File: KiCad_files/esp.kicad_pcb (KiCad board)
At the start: 2 copper layers, 86 x 75 mm, 69 parts, among them J1 Conn_01x02_Pin, J2 USB4105-GF-A, J3 Conn_01x16_Pin, Q2 DMP3099L, SW1 SLW-171175-7A-N-D, U1 B3U-1000P, U12 ESP32-S3-MINI-1U, U13 BNO085, U2 1060, U7 LTC4412xS6

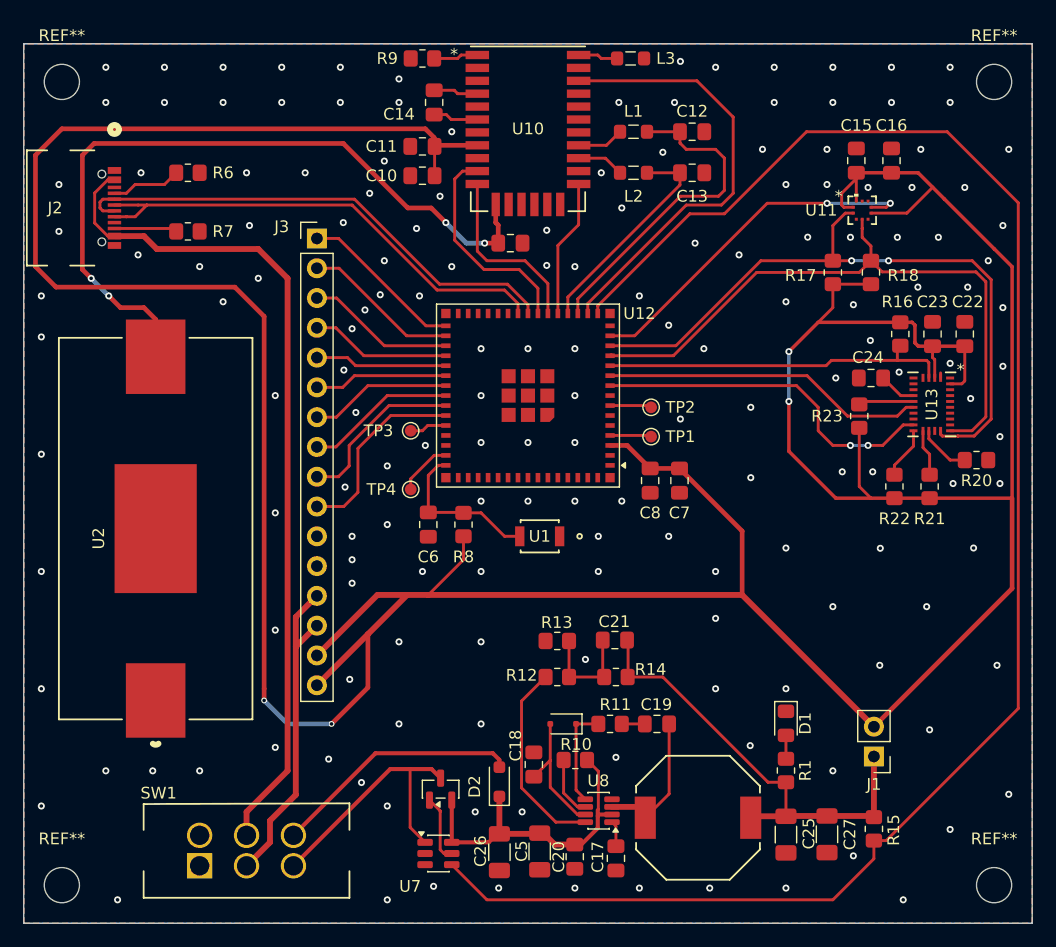
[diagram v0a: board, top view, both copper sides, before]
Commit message: power supply FB circuitry to better place
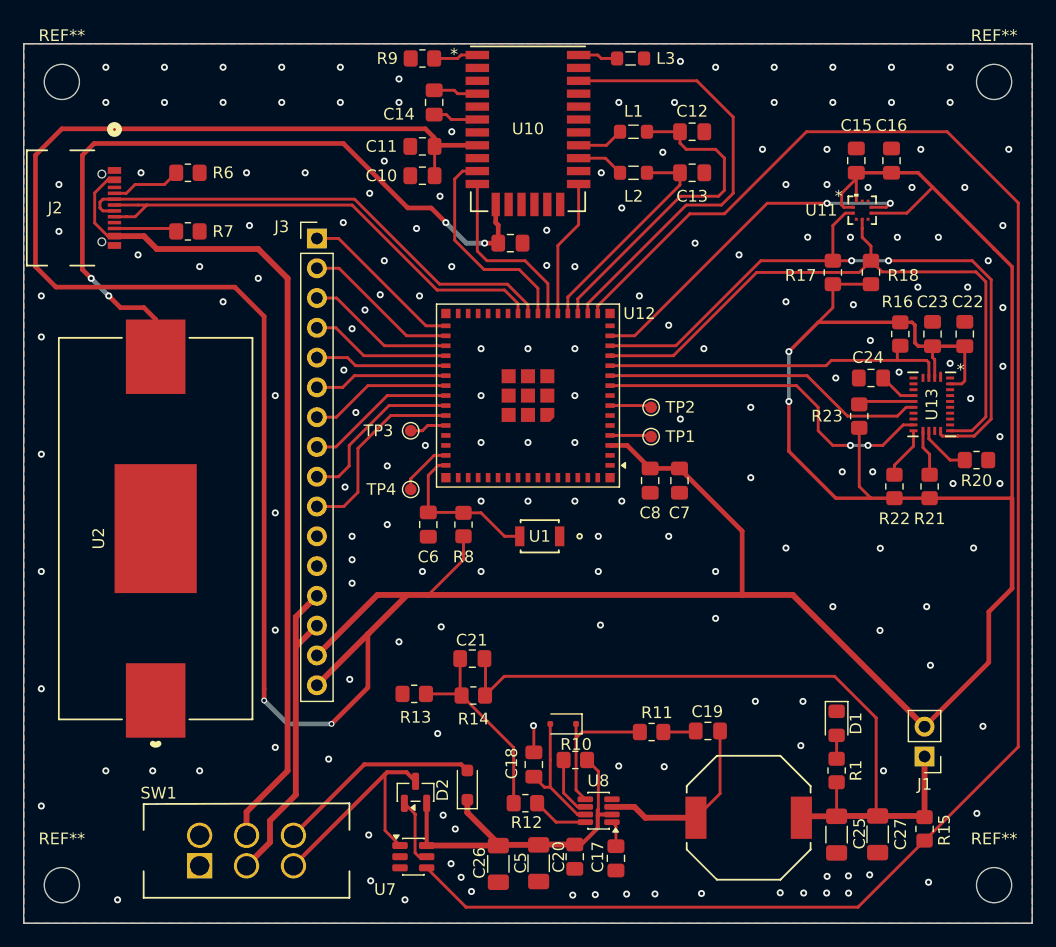
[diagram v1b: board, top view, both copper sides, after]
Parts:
- moved R13 13.0 mm to (115.3, 80.4)
- moved C21 12.3 mm to (120.3, 77.4)
- moved R14 12.3 mm to (120.3, 80.6)
- moved R12 11.1 mm to (124.8, 89.8), turned to 180 degrees
- moved C19 4.38 mm to (140.3, 83.6)
- moved C25 4.32 mm to (151.3, 92.4)
- moved C27 4.32 mm to (154.8, 92.4)
- moved D1 4.32 mm to (151.3, 83.0)
- moved J1 4.32 mm to (158.8, 85.8)
- moved L4 4.32 mm to (143.8, 91.0)
- moved R1 4.32 mm to (151.3, 87.0)
- moved R15 4.32 mm to (158.8, 92.0)
- moved R11 3.61 mm to (135.5, 83.7)
- moved D2 2.75 mm to (119.8, 88.2)
- moved Q2 2.16 mm to (115.4, 88.8)
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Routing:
- net Net-(J1-Pin_1): track 38.2 -> 64.9 mm
- net Net-(R12-Pad1): track 16.9 -> 4.78 mm
- net Net-(C21-Pad1): track 9.10 -> 17.1 mm
- net Net-(U8-SW): track 10.8 -> 15.8 mm
- net Net-(D3-K): track 8.65 -> 12.5 mm
- net Net-(D2-K): track 27.5 -> 31.3 mm
- net Net-(D2-A): track 21.3 -> 17.6 mm
- net /BAT_STAT: track 145.5 -> 149.1 mm
- net +3.3V: track 353.8 -> 356.3 mm
- net Net-(Q2-D): track 23.1 -> 20.6 mm
- net GND: track 1.09 -> 3.38 mm, vias 168 -> 176
- net Net-(C19-Pad2): track 1.96 -> 2.80 mm

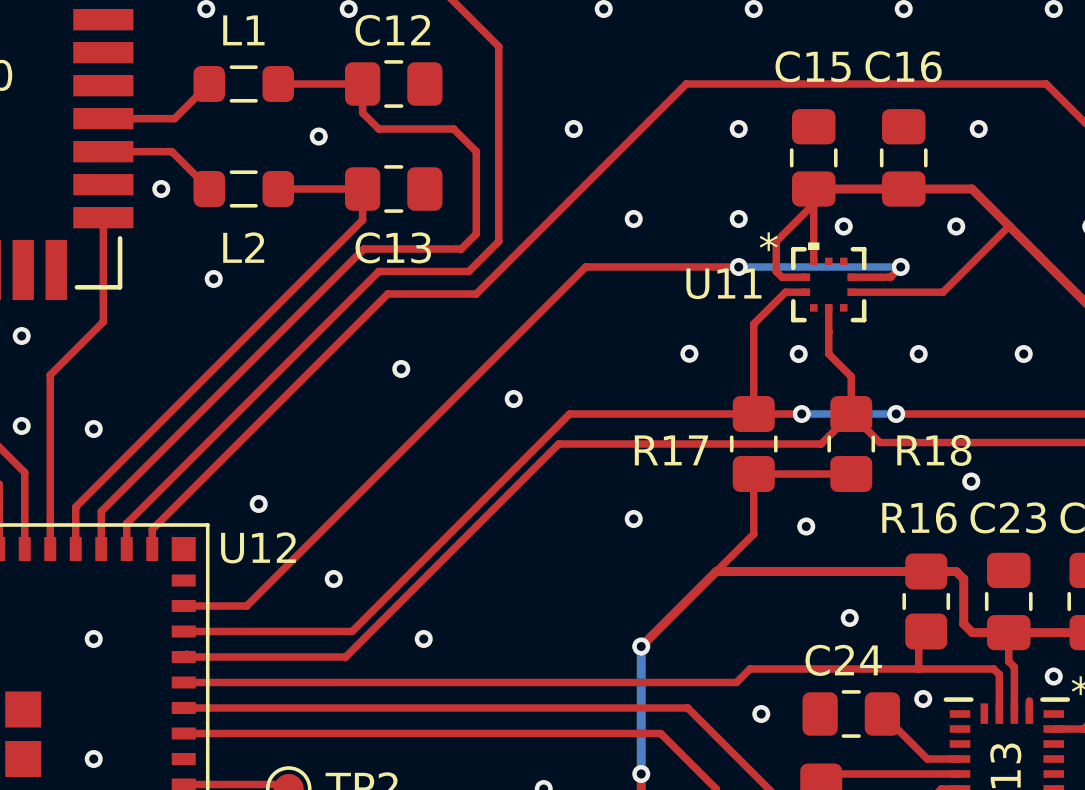
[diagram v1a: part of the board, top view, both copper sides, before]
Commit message: barometri interrupt viety muualta kuin sirun alta
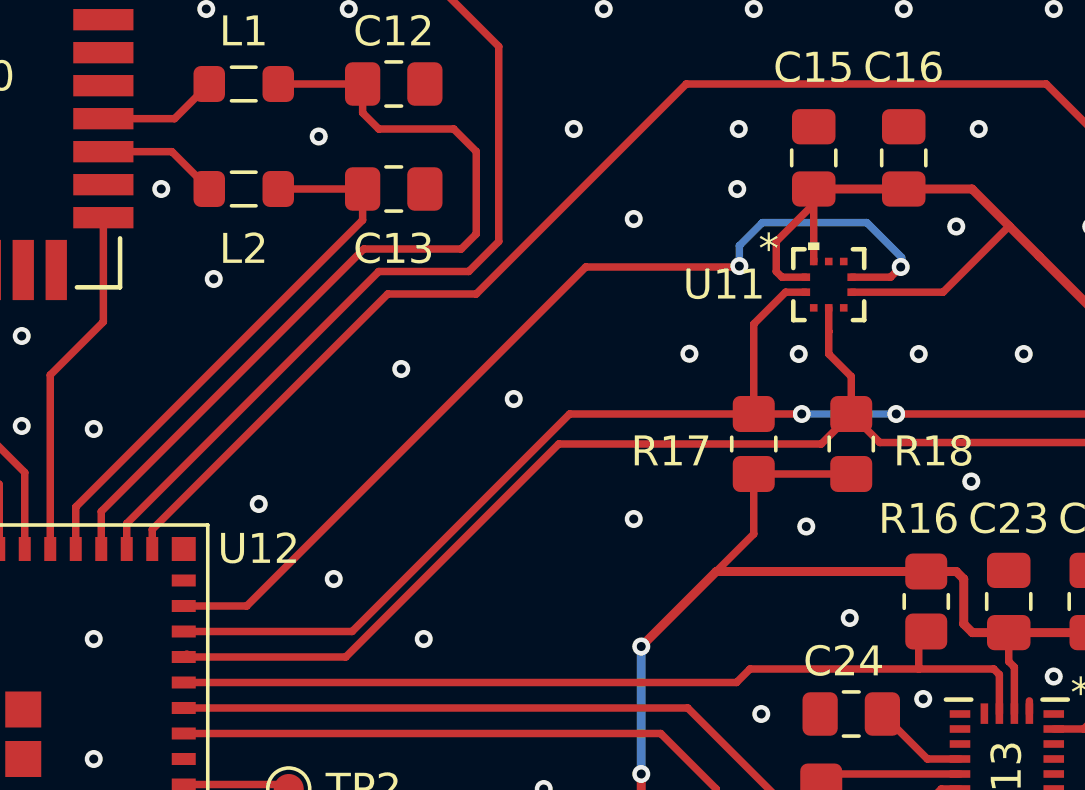
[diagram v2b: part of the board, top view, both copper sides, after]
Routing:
- net /BAROMETER_INT: track 30.4 -> 32.2 mm
- net GND: vias 176 -> 175
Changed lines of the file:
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@@
 	)
 	(via
-		(at 154 37.25)
-		(size 0.6)
-		(drill 0.3)
-		(layers "F.Cu" "B.Cu")
-		(net 1)
-	)
-	(via
 		(at 111.1 47.7)
 		(size 0.6)
@@
 	)
 	(via
+		(at 150.45 36)
+		(size 0.6)
+		(drill 0.3)
+		(layers "F.Cu" "B.Cu")
+		(free yes)
+		(net 1)
+	)
+	(via
 		(at 117.5 38)
 		(size 0.6)
@@
 	)
 	(via
-		(at 150.5 37)
-		(size 0.6)
-		(drill 0.3)
-		(layers "F.Cu" "B.Cu")
-		(net 1)
-	)
-	(via
 		(at 97 44)
 		(size 0.6)
@@
 	)
 	(segment
-		(start 134.1 49.9)
-		(end 145.4 38.6)
+		(start 150.52 38.57)
+		(end 150.49 38.6)
 		(width 0.25)
 		(layer "F.Cu")
@@
 	(segment
 		(start 145.4 38.6)
-		(end 150.5 38.6)
+		(end 134.1 49.9)
 		(width 0.25)
 		(layer "F.Cu")
@@
 	)
 	(segment
-		(start 132 49.9)
-		(end 134.1 49.9)
+		(start 134.1 49.9)
+		(end 132 49.9)
 		(width 0.25)
 		(layer "F.Cu")
@@
 	)
 	(segment
+		(start 150.49 38.6)
+		(end 145.4 38.6)
+		(width 0.25)
+		(layer "F.Cu")
+		(net 52)
+	)
+	(segment
 		(start 155.560501 38.939499)
 		(end 155.9 38.6)
@@
 	)
 	(via
-		(at 150.5 38.6)
+		(at 150.52 38.57)
 		(size 0.6)
 		(drill 0.3)
@@
 	)
 	(segment
-		(start 150.5 38.6)
-		(end 155.9 38.6)
+		(start 155.9 38.6)
+		(end 155.92 38.6)
+		(width 0.25)
+		(layer "B.Cu")
+		(net 52)
+	)
+	(segment
+		(start 155.92 38.6)
+		(end 155.93 38.61)
+		(width 0.25)
+		(layer "B.Cu")
+		(net 52)
+	)
+	(segment
+		(start 155.93 38.61)
+		(end 155.93 38.28)
+		(width 0.25)
+		(layer "B.Cu")
+		(net 52)
+	)
+	(segment
+		(start 150.52 37.89)
+		(end 150.52 38.57)
+		(width 0.25)
+		(layer "B.Cu")
+		(net 52)
+	)
+	(segment
+		(start 154.77 37.12)
+		(end 151.29 37.12)
+		(width 0.25)
+		(layer "B.Cu")
+		(net 52)
+	)
+	(segment
+		(start 151.29 37.12)
+		(end 150.52 37.89)
+		(width 0.25)
+		(layer "B.Cu")
+		(net 52)
+	)
+	(segment
+		(start 155.93 38.28)
+		(end 154.77 37.12)
 		(width 0.25)
 		(layer "B.Cu")

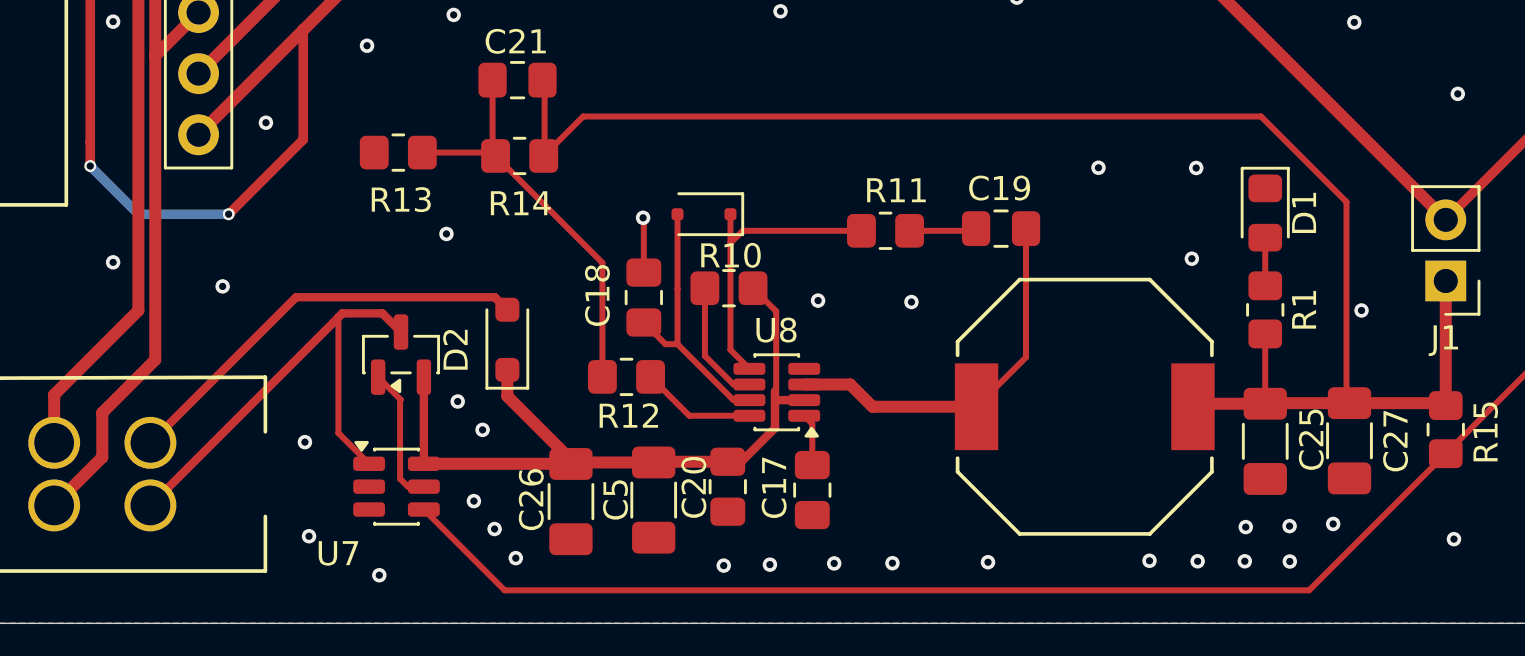
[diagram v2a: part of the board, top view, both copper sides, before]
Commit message: fixed via positions and power trace width
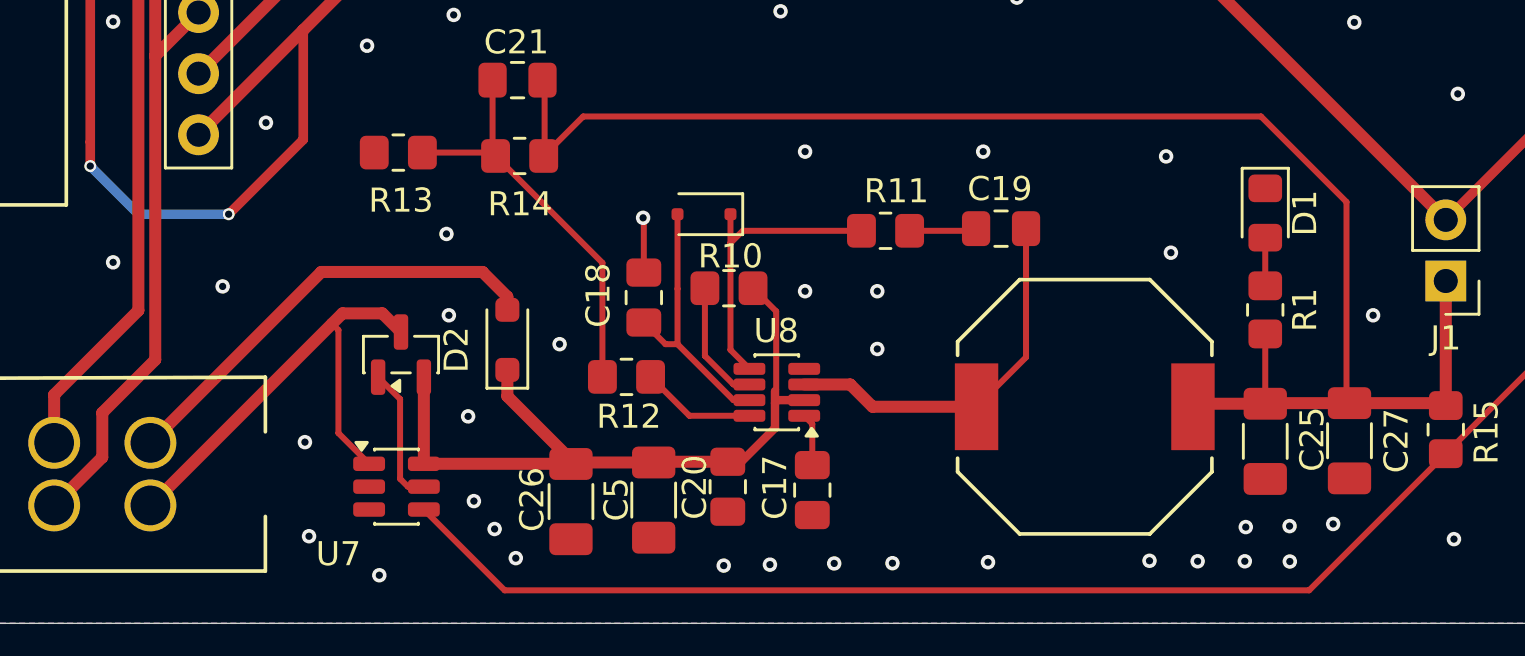
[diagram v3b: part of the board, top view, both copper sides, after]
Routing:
- net Net-(D2-A): track 17.6 -> 18.7 mm
- net GND: vias 175 -> 178
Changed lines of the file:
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@@
 	)
 	(via
+		(at 132.2 80.4)
+		(size 0.6)
+		(drill 0.3)
+		(layers "F.Cu" "B.Cu")
+		(net 1)
+	)
+	(via
 		(at 152.33 95.96)
 		(size 0.6)
@@
 	)
 	(via
-		(at 132.74 86.59)
+		(at 132.2 86.2)
 		(size 0.6)
 		(drill 0.3)
@@
 	)
 	(via
-		(at 148.45 81.08)
+		(at 147.2 80.6)
 		(size 0.6)
 		(drill 0.3)
@@
 	)
 	(via
+		(at 135.2 88.6)
+		(size 0.6)
+		(drill 0.3)
+		(layers "F.Cu" "B.Cu")
+		(net 1)
+	)
+	(via
 		(at 151 73)
 		(size 0.6)
@@
 	)
 	(via
-		(at 117.7675 90.7825)
+		(at 117.4 87.2)
 		(size 0.6)
 		(drill 0.3)
@@
 	)
 	(via
-		(at 144.39 81.07)
+		(at 139.6 80.4)
 		(size 0.6)
 		(drill 0.3)
@@
 	)
 	(via
-		(at 148.27 84.85)
+		(at 147.4 84.6)
 		(size 0.6)
 		(drill 0.3)
@@
 	)
 	(via
+		(at 122 88.4)
+		(size 0.6)
+		(drill 0.3)
+		(layers "F.Cu" "B.Cu")
+		(net 1)
+	)
+	(via
 		(at 162.75 55.25)
 		(size 0.6)
@@
 	)
 	(via
-		(at 136.62 86.65)
+		(at 135.2 86.2)
 		(size 0.6)
 		(drill 0.3)
@@
 	)
 	(via
-		(at 155.32 87)
+		(at 155.8 87.2)
 		(size 0.6)
 		(drill 0.3)
@@
 	)
 	(via
-		(at 118.8 91.96)
+		(at 118.2 91.4)
 		(size 0.6)
 		(drill 0.3)
@@
 		(start 116.361249 89.77)
 		(end 116.361249 93.37)
-		(width 0.35)
+		(width 0.5)
 		(layer "F.Cu")
 		(net 2)
@@
 	)
 	(segment
-		(start 105 92.5)
-		(end 111.05 86.45)
-		(width 0.35)
+		(start 119.83 86.43)
+		(end 119.83 86.97)
+		(width 0.5)
 		(layer "F.Cu")
 		(net 17)
 	)
 	(segment
-		(start 111.05 86.45)
-		(end 119.31 86.45)
-		(width 0.35)
+		(start 118.8 85.4)
+		(end 119.83 86.43)
+		(width 0.5)
 		(layer "F.Cu")
 		(net 17)
 	)
 	(segment
-		(start 119.31 86.45)
-		(end 119.83 86.97)
-		(width 0.35)
+		(start 112.1 85.4)
+		(end 118.8 85.4)
+		(width 0.5)
+		(layer "F.Cu")
+		(net 17)
+	)
+	(segment
+		(start 105 92.5)
+		(end 112.1 85.4)
+		(width 0.5)
 		(layer "F.Cu")
 		(net 17)
@@
 	)
 	(segment
-		(start 115.397749 90.7065)
-		(end 115.373749 90.7305)
+		(start 115.373749 90.6825)
+		(end 114.461249 89.77)
 		(width 0.25)
 		(layer "F.Cu")
@@
 	)
 	(segment
-		(start 114.461249 89.77)
-		(end 115.397749 90.7065)
+		(start 115.373749 93.994999)
+		(end 115.69875 94.32)
 		(width 0.25)
 		(layer "F.Cu")
@@
 	(segment
 		(start 115.373749 93.994999)
-		(end 115.69875 94.32)
+		(end 115.373749 90.6825)
 		(width 0.25)
 		(layer "F.Cu")
@@
 	)
 	(segment
-		(start 115.373749 90.7305)
-		(end 115.373749 93.994999)
+		(start 112.811249 92.095)
+		(end 112.811249 87.811249)
 		(width 0.25)
 		(layer "F.Cu")
-		(net 31)
+		(net 32)
 	)
 	(segment
-		(start 112.811249 87.288751)
-		(end 105 95.1)
-		(width 0.35)
+		(start 114.636249 87.12)
+		(end 112.98 87.12)
+		(width 0.5)
 		(layer "F.Cu")
 		(net 32)
@@
 	(segment
 		(start 112.98 87.12)
-		(end 112.811249 87.288751)
-		(width 0.35)
+		(end 112.55 87.55)
+		(width 0.5)
 		(layer "F.Cu")
 		(net 32)
 	)
 	(segment
-		(start 114.086249 93.37)
-		(end 112.811249 92.095)
+		(start 112.811249 87.811249)
+		(end 112.55 87.55)
 		(width 0.25)
 		(layer "F.Cu")
@@
 	)
 	(segment
-		(start 114.636249 87.12)
-		(end 112.98 87.12)
-		(width 0.35)
+		(start 114.086249 93.37)
+		(end 112.811249 92.095)
+		(width 0.25)
 		(layer "F.Cu")
 		(net 32)
 	)
 	(segment
-		(start 115.411249 87.895)
-		(end 114.636249 87.12)
-		(width 0.35)
+		(start 112.55 87.55)
+		(end 105 95.1)
+		(width 0.5)
 		(layer "F.Cu")
 		(net 32)
 	)
 	(segment
-		(start 112.811249 92.095)
-		(end 112.811249 87.288751)
-		(width 0.25)
+		(start 115.411249 87.895)
+		(end 114.636249 87.12)
+		(width 0.5)
 		(layer "F.Cu")
 		(net 32)
